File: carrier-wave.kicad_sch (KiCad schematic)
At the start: 10 parts, among them J1 USB C 2.0, U1 ATSAMD21E18A-M

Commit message: Updated Drawing Sheets
Added Shell Logo and OSHW Logo. Changed Rev. from 1.0 to A
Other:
- title: Portable Function Generator -> Carrier-Wave

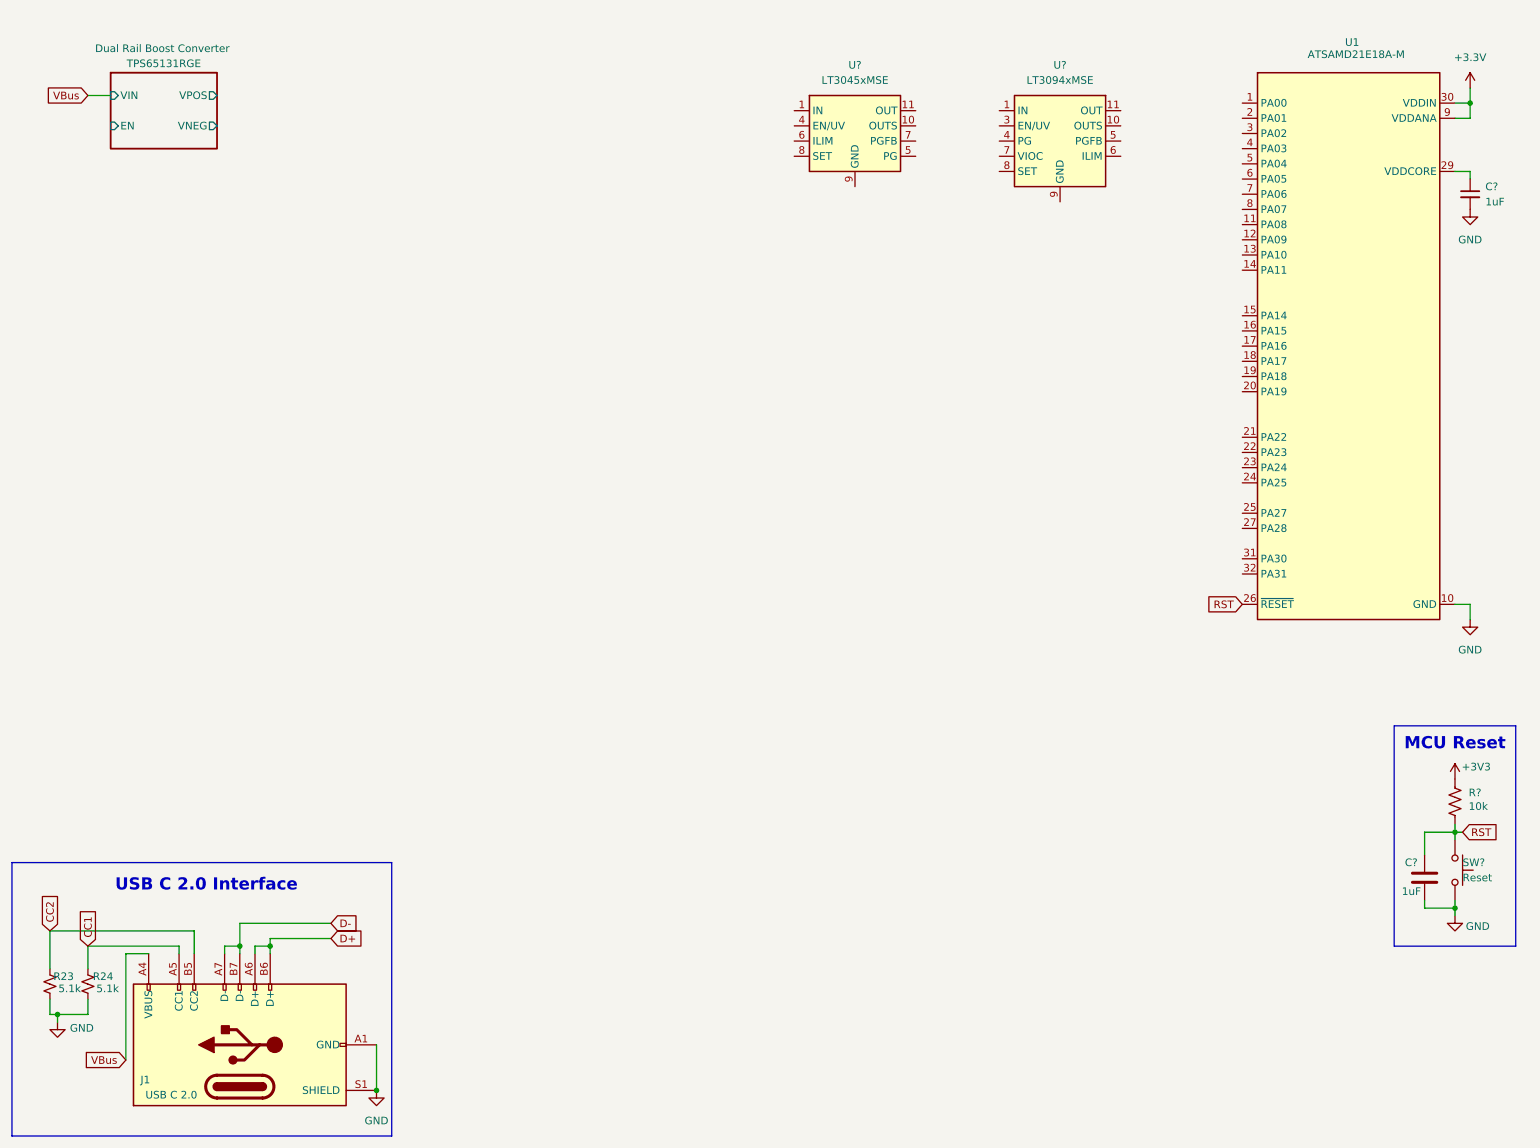
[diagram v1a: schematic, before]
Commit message: MCU LDO & Inputs
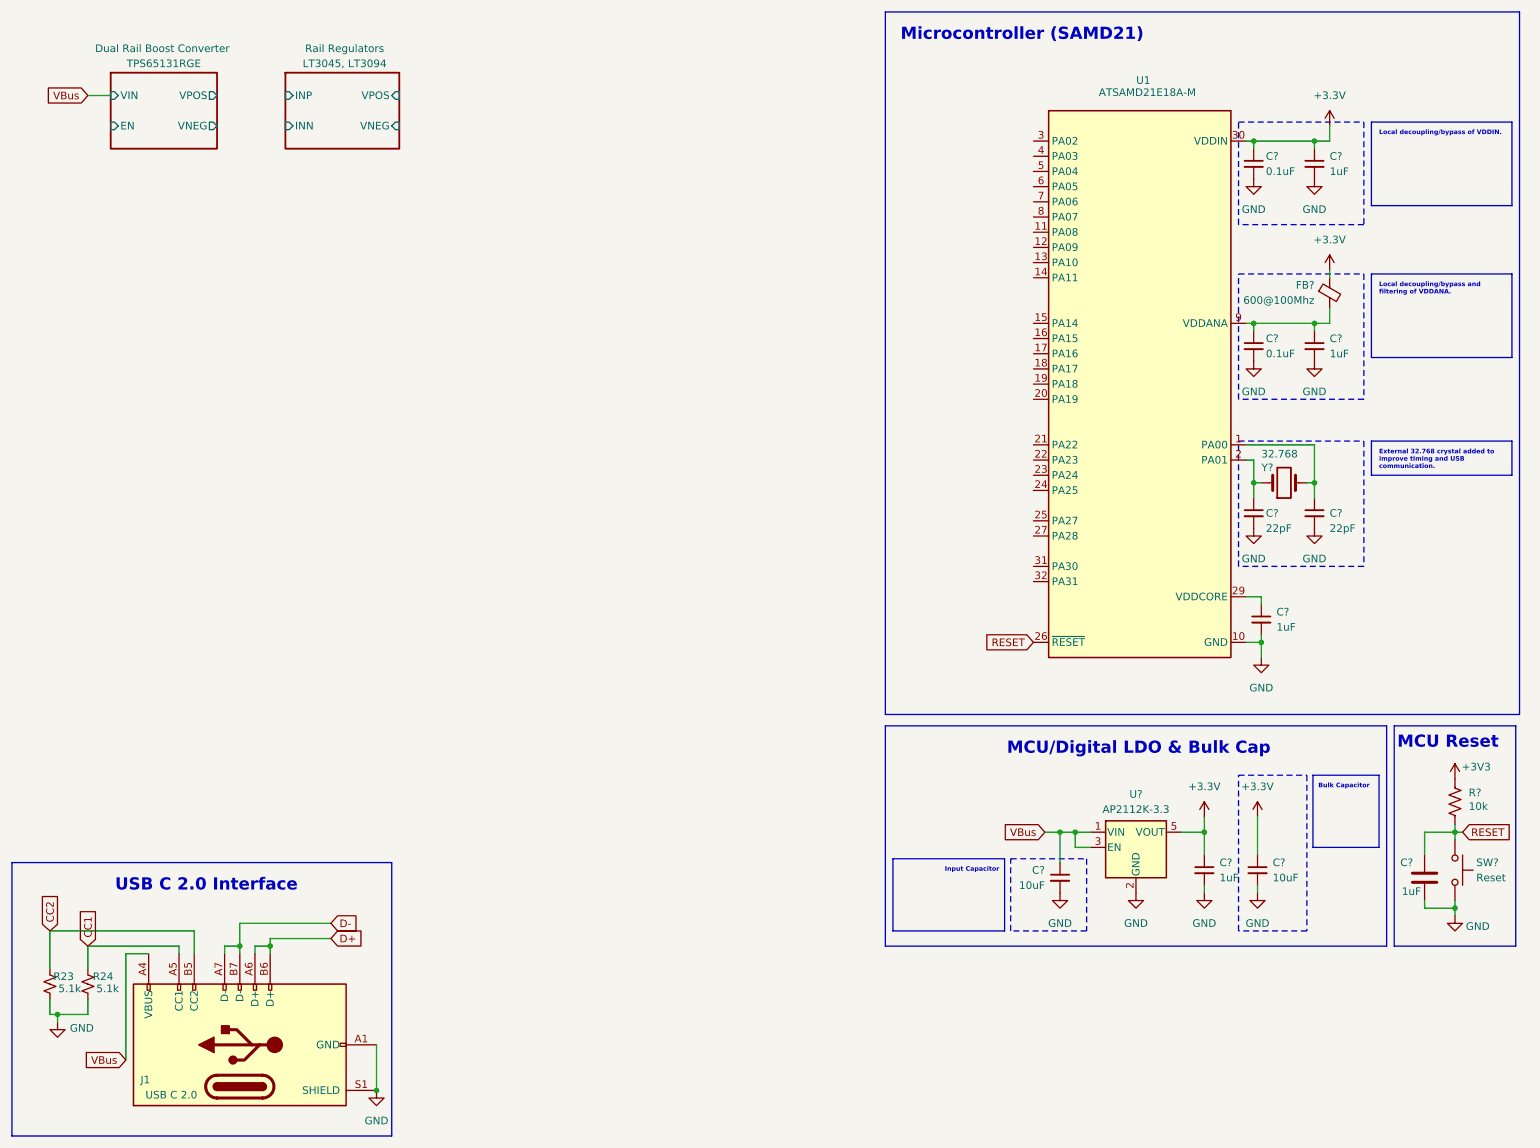
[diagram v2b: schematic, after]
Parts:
- removed U?: LT3045xMSE, Package_SO:MSOP-12-1EP_3x4.039mm_P0.65mm_EP1.651x2.845mm, symbol Regulator_Linear:LT3045xMSE
- removed U?: LT3094xMSE, Package_SO:MSOP-12-1EP_3x4.039mm_P0.65mm_EP1.651x2.845mm, symbol Regulator_Linear:LT3094xMSE
- added C? (x2): 22pF, symbol Device:C_Small
- added C? (x3): 1uF, symbol Device:C_Small
- added C? (x2): 10uF, symbol Device:C_Small
- added C? (x2): 0.1uF, symbol Device:C_Small
- added FB?: 600@100Mhz, symbol Device:FerriteBead_Small
- added U?: AP2112K-3.3, Package_TO_SOT_SMD:SOT-23-5, symbol Regulator_Linear:AP2112K-3.3
- added Y?: 32.768, symbol Device:Crystal
- SW?: footprint Button_Switch_SMD:SW_SPST_CK_RS282G05A3 -> Button_Switch_SMD:SW_SPST_PTS810
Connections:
- net +3.3V: now also C?.1, C?.1, C?.1, C?.1, FB?.1, U?.5 (VOUT); no longer U1.9 (VDDANA)
- net GND: now also C?.2, C?.2, C?.2, C?.2, C?.2, C?.2, C?.2, C?.2, C?.2, U?.2 (GND)
- net VBus: now also C?.1, U?.1 (VIN), U?.3 (EN)
- net at U1.1 (PA00): now also C?.1, Y?.2
- net at U1.2 (PA01): now also C?.1, Y?.1
- net RST renamed RESET
- new net: C?.1, C?.1, FB?.2, U1.9 (VDDANA)
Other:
- added sheet Rail Regulators (linear_regulators.kicad_sch)
- note added: "Bulk Capacitor"
- note added: "External 32.768 crystal added to improve timing and USB communication."
- note added: "Input Capacitor"
- note added: "Local decoupling/bypass and filtering of VDDANA."
- note added: "Local decoupling/bypass of VDDIN."
- note added: "MCU/Digital LDO & Bulk Cap"
- note added: "Microcontroller (SAMD21)"
- moved on the sheet: C?, U1

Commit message: Added USB-C ESD Protection
Added TVS diode array, ferrite bead on VBUS, and 10uF bulk cap.
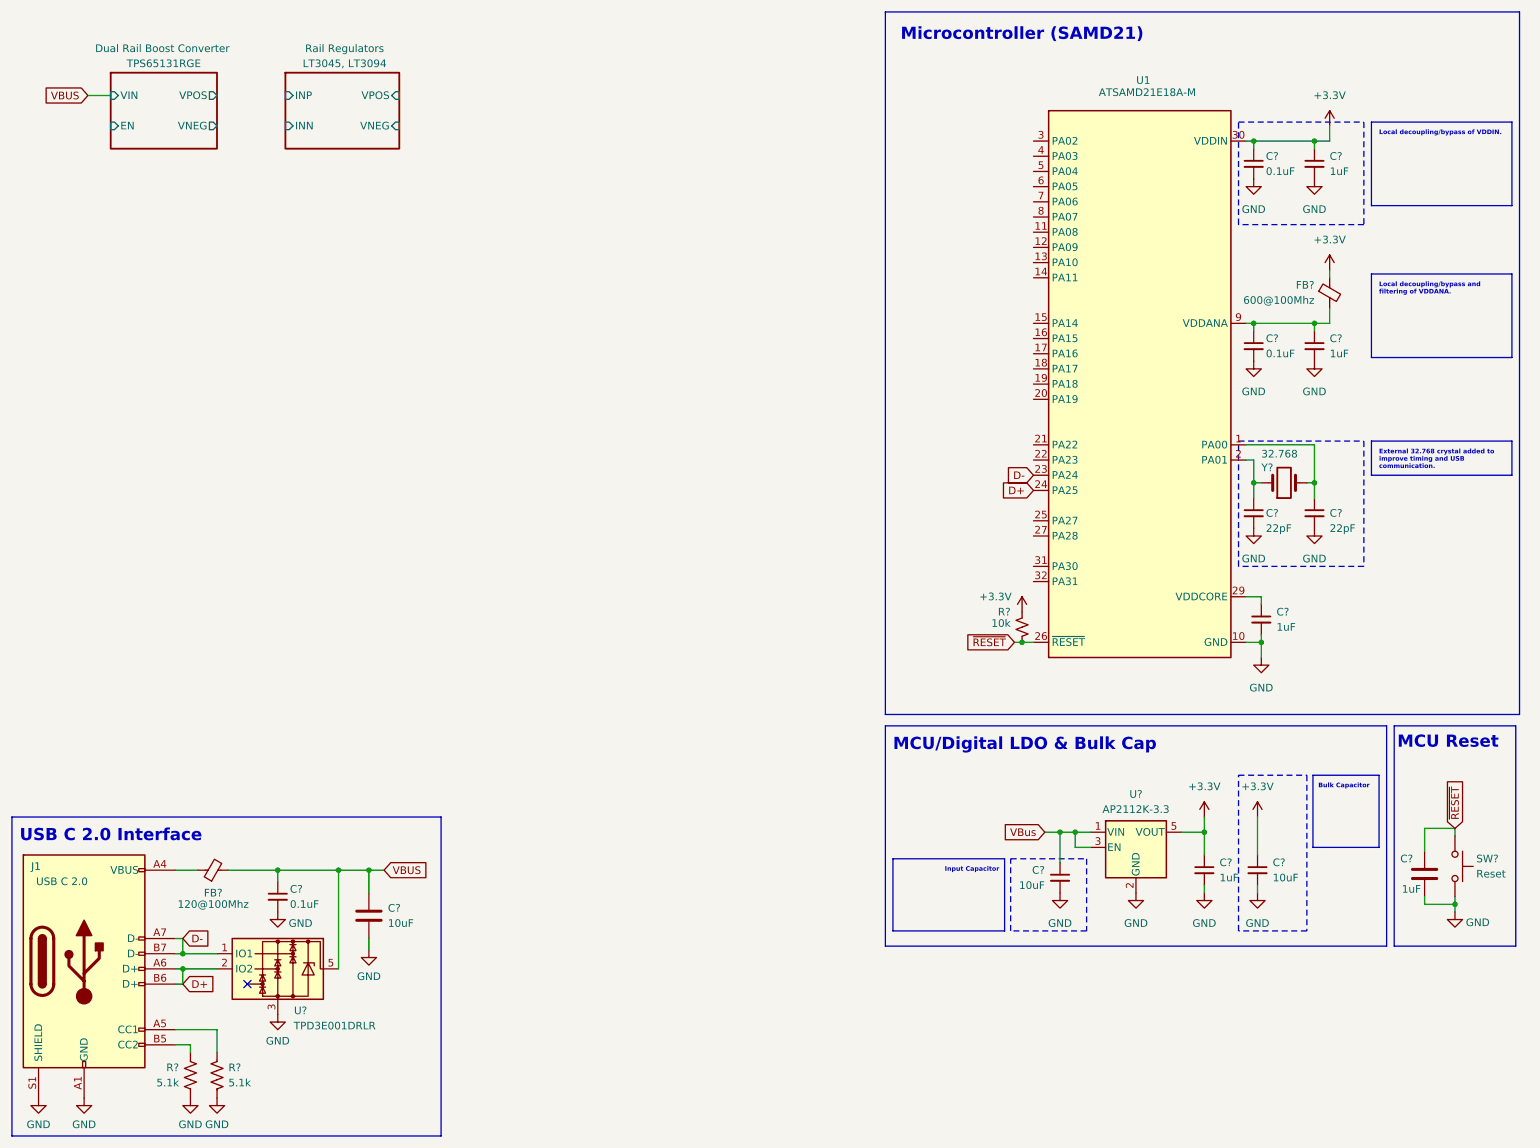
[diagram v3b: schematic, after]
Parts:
- removed R23, R24: 5.1k, Resistor_SMD:R_0805_2012Metric_Pad1.20x1.40mm_HandSolder, symbol Device:R_Small_US
- removed R?: 10k, Resistor_SMD:R_0805_2012Metric_Pad1.20x1.40mm_HandSolder, symbol Device:R_US
- added C?: 10uF, symbol Device:C
- added C?: 0.1uF, symbol Device:C_Small
- added FB?: 120@100Mhz, Inductor_SMD:L_0805_2012Metric_Pad1.05x1.20mm_HandSolder, symbol Device:FerriteBead_Small
- added R? (x2): 5.1k, symbol Device:R_US
- added R?: 10k, symbol Device:R_Small_US
- added U?: TPD3E001DRLR, Package_TO_SOT_SMD:SOT-553, symbol Power_Protection:TPD3E001DRLR
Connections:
- net +3.3V: now also R?.1
- net D+: now also U1.24 (PA25), U?.2 (IO2)
- net D-: now also U1.23 (PA24), U?.1 (IO1)
- net GND: now also C?.2, C?.2, R?.2, R?.2, U?.3
- net VBus: no longer J1.A4 (VBUS), J1.A9 (VBUS), J1.B4 (VBUS), J1.B9 (VBUS)
- net CC1: no longer names the net of J1.A5 (CC1)
- net CC1: now also R?.1
- net CC2: no longer names the net of J1.B5 (CC2)
- net CC2: now also R?.1
- net RESET renamed ~{RESET}
- net ~{RESET}: now also R?.2
- new net: FB?.1, J1.A4 (VBUS), J1.A9 (VBUS), J1.B4 (VBUS), J1.B9 (VBUS)
- new net VBUS: C?.1, C?.1, FB?.2, U?.5
- no-connect marks 0 -> 1
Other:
- moved on the sheet: C?, J1, SW?

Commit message: USB Filtering Adjustments
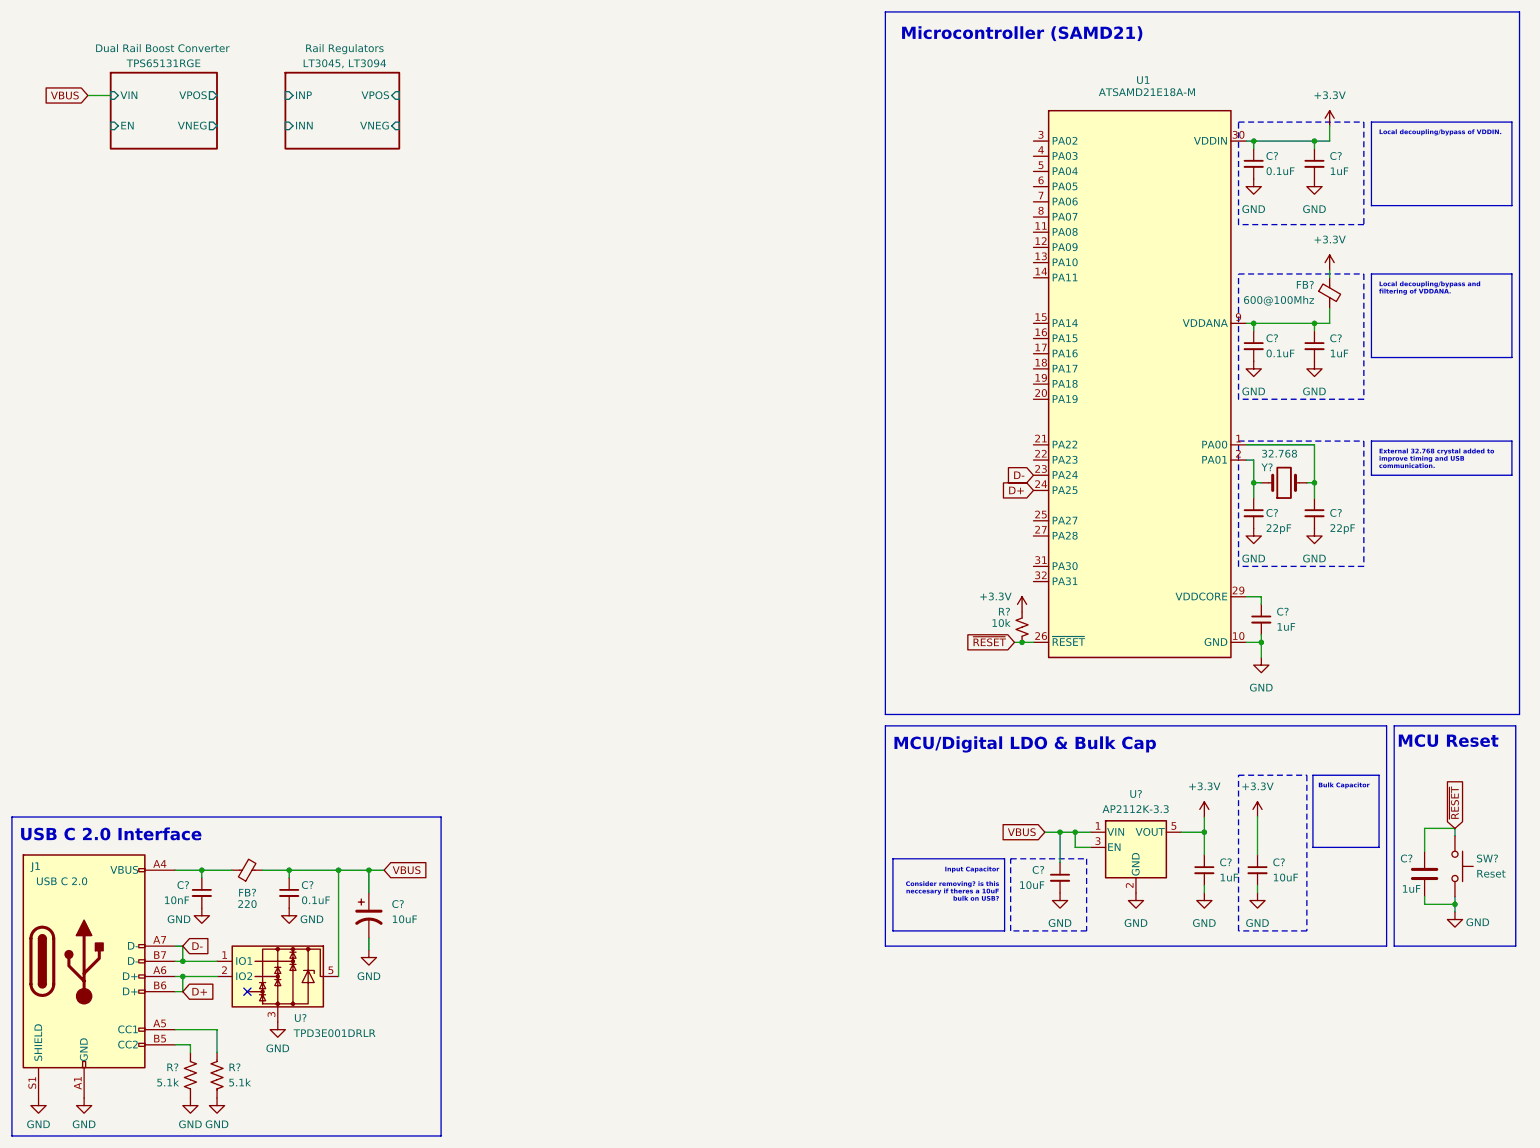
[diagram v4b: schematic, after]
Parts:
- removed C?: 10uF, symbol Device:C
- added C?: 10uF, HIGHER ESR ELECTROLYTIC, symbol Device:C_Polarized_US
- added C?: 10nF, symbol Device:C_Small
- FB?: value 120@100Mhz -> 220; footprint Inductor_SMD:L_0805_2012Metric_Pad1.05x1.20mm_HandSolder -> Inductor_SMD:L_0603_1608Metric_Pad1.05x0.95mm_HandSolder
- FB?: footprint (none) -> Inductor_SMD:L_0603_1608Metric
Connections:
- net VBus is gone; now on net VBUS: C?.1, U?.1 (VIN), U?.3 (EN)
- net GND: now also C?.2, C?.2
- net VBUS: now also C?.1
- net at FB?.1, J1.A4 (VBUS), J1.A9 (VBUS)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: now also C?.1
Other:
- note added: "Input Capacitor Consider removing? is this neccesary if theres a 10uF bulk on USB?"
- note removed: "Input Capacitor"
- moved on the sheet: C?, FB?, U?

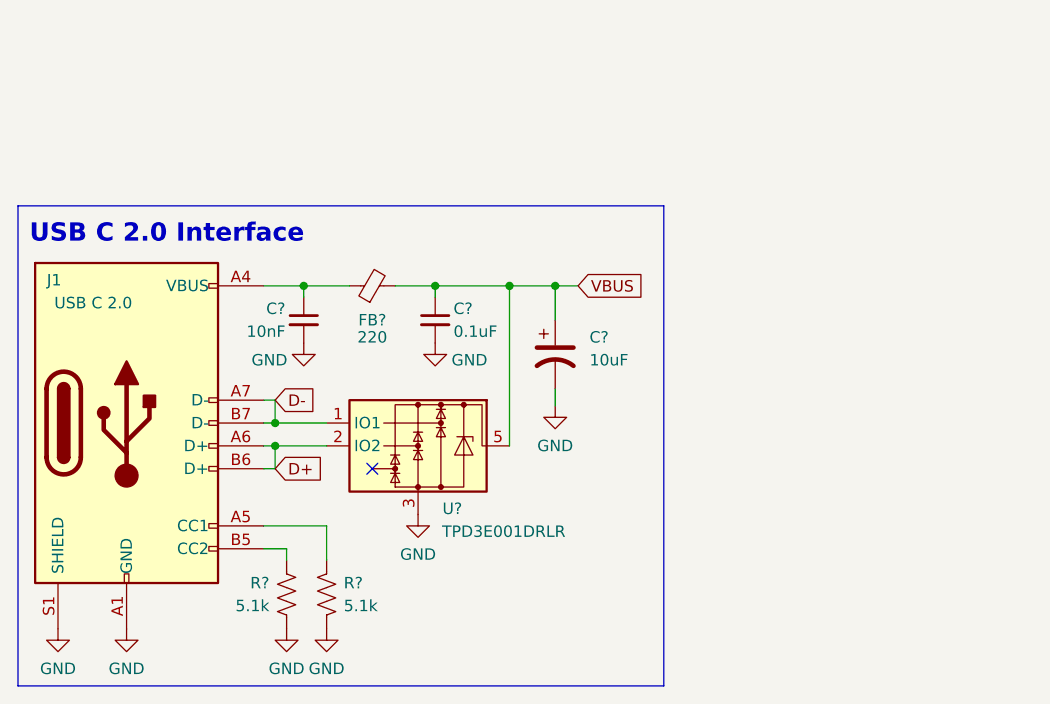
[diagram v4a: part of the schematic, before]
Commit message: Moved VBUS TVS
put VBUS TVS before any other components. Added notes about VBUS soft start and necessity of pi filter
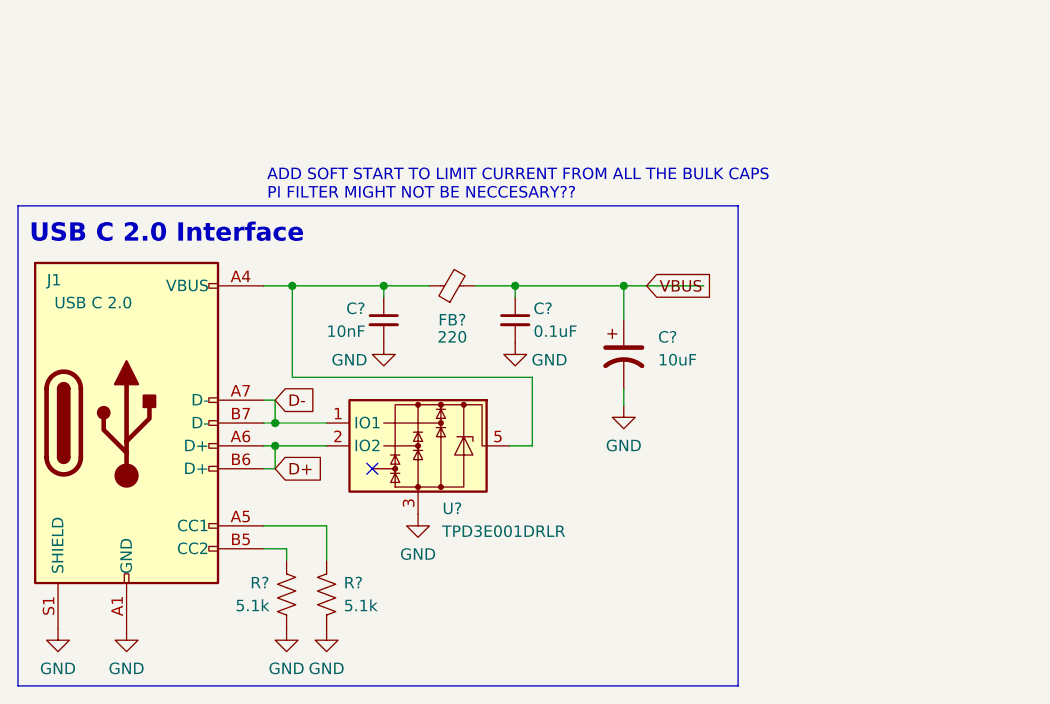
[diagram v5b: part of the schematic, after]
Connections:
- net VBUS: no longer U?.5
- net at C?.1, FB?.1, J1.A4 (VBUS)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: now also U?.5
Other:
- note added: "ADD SOFT START TO LIMIT CURRENT FROM ALL THE BULK CAPS PI FILTER MIGHT NOT BE NECCESARY??"
- moved on the sheet: C?, FB?

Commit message: Update USB C Frontend
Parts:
- removed U?: TPD3E001DRLR, Package_TO_SOT_SMD:SOT-553, symbol Power_Protection:TPD3E001DRLR
- added U?: USBLC6-2SC6, Package_TO_SOT_SMD:SOT-23-6_Handsoldering, symbol Power_Protection:USBLC6-2SC6
- added U?: STM32G0B0CETx, Package_QFP:LQFP-48_7x7mm_P0.5mm, symbol MCU_ST_STM32G0:STM32G0B0CETx
- C?: value 10uF -> 4.7uF
- FB?: value 220 -> 470@100Mhz
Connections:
- net D+: now also U?.4 (I/O2); no longer J1.A6 (D+), J1.B6 (D+)
- net D-: now also U?.6 (I/O1); no longer J1.A7 (D-), J1.B7 (D-)
- net GND: now also U?.2 (GND)
- net at C?.1, FB?.1, J1.A4 (VBUS)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: now also U?.5 (VBUS)
- new net: J1.A6 (D+), J1.B6 (D+), U?.3 (I/O2)
- new net: J1.A7 (D-), J1.B7 (D-), U?.1 (I/O1)
- no-connect marks 1 -> 0
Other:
- note added: "ADD SOFT START TO LIMIT CURRENT FROM ALL THE BULK CAPS"
- note added: "Microcontroller (STM32G0)"
- note removed: "ADD SOFT START TO LIMIT CURRENT FROM ALL THE BULK CAPS PI FILTER MIGHT NOT BE NECCESARY??"
- note removed: "Microcontroller (SAMD21)"
- moved on the sheet: C?
